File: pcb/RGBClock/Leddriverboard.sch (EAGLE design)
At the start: 37 parts, among them U1 LP3878MR-ADJ, U2 P82B96DR, U3 PCA9685PW, U4 ZXLD1362ET5TA, U5 ZXLD1362ET5TA, U6 ZXLD1362ET5TA, X1 5566-4

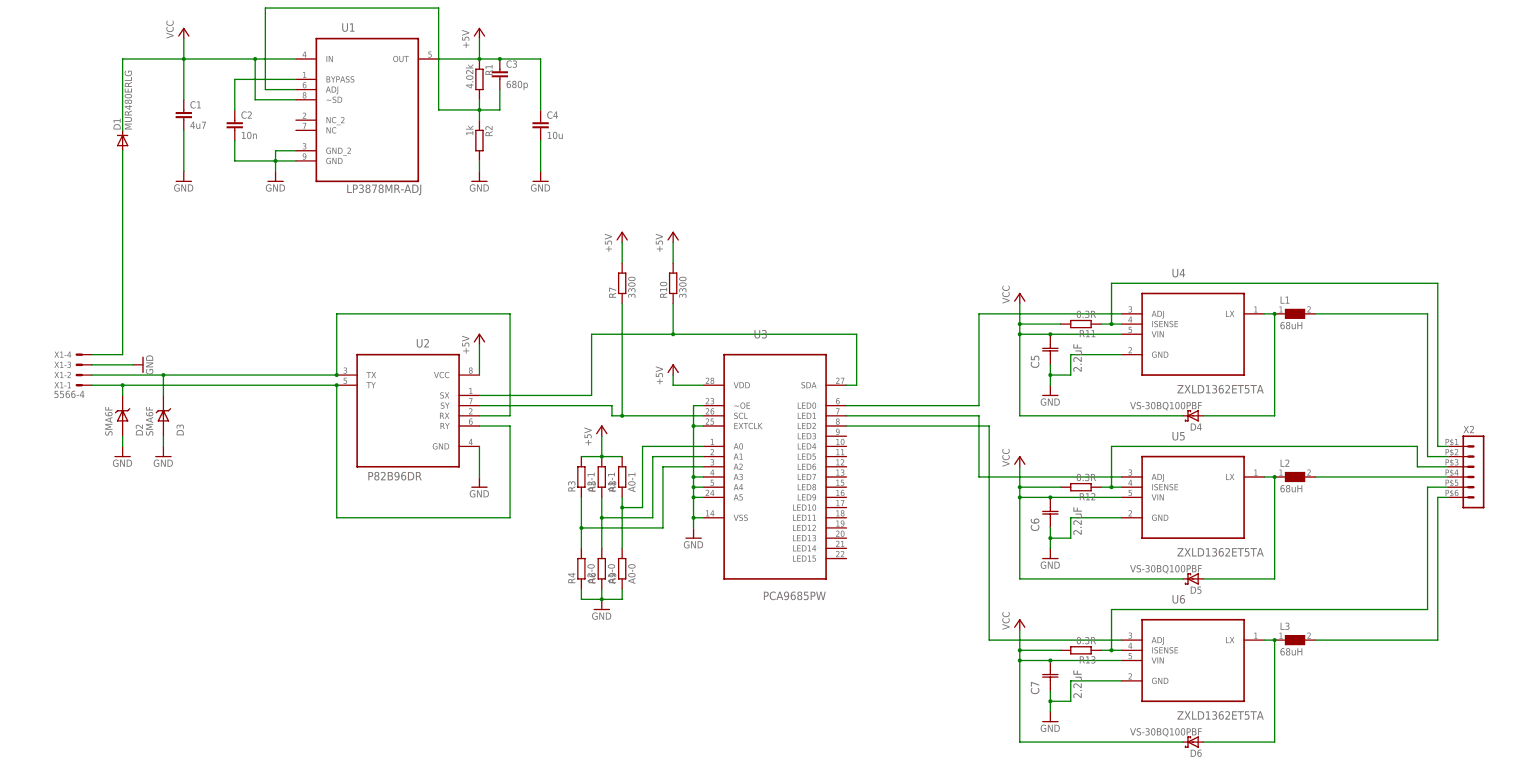
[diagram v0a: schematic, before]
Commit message: 
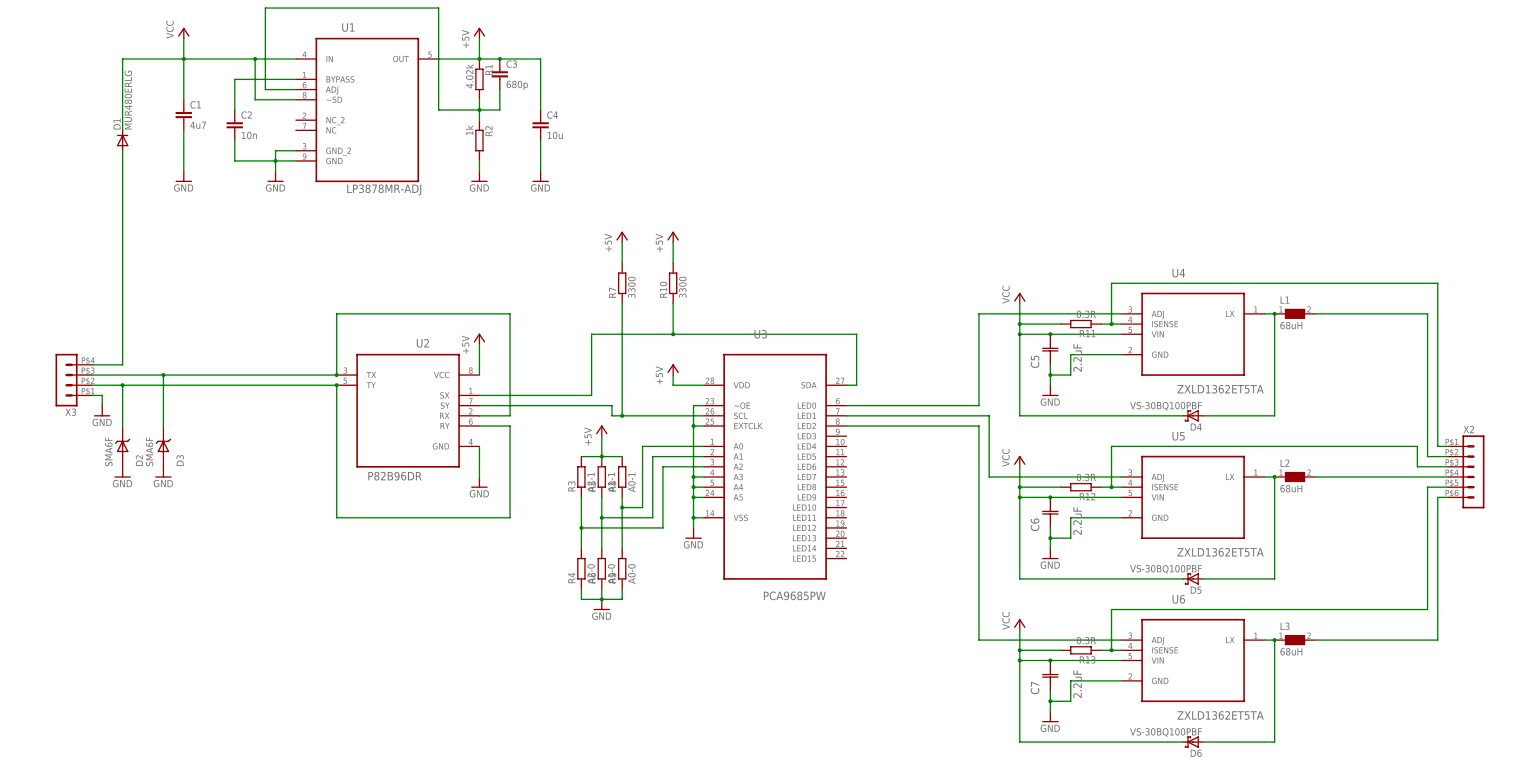
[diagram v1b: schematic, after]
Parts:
- removed X1: 5566-4, con-molex:5566-4
- added X3: (no value), con-molex-micro-fit-3_0:HEADER_POS4_43045-0401
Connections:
- net GND: now also X3.1; no longer X1-3.S
- net N$22: now also X3.2; no longer X1-1.S
- net N$25: now also X3.4; no longer X1-4.S
- net N$7: now also X3.3; no longer X1-2.S
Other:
- moved on the sheet: D2, D3
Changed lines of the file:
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@@
 <part name="GND14" library="supply1" deviceset="GND" device=""/>
 <part name="P+6" library="supply1" deviceset="+5V" device=""/>
-<part name="X1" library="con-molex" deviceset="5566-4" device=""/>
 <part name="D3" library="MyComponents" deviceset="SMA6F" device=""/>
 <part name="D2" library="MyComponents" deviceset="SMA6F" device=""/>
@@
 <part name="U1" library="Texas" deviceset="LP3878MR-ADJ" device=""/>
 <part name="P+3" library="supply1" deviceset="+5V" device=""/>
-<part name="GND15" library="supply1" deviceset="GND" device=""/>
 <part name="GND16" library="supply1" deviceset="GND" device=""/>
 <part name="C1" library="rcl" deviceset="C-EU" device="C1206" value="4u7"/>
@@
 <part name="R4" library="resistor" deviceset="R-EU_" device="R0402" value="A2-0"/>
 <part name="P+5" library="supply1" deviceset="+5V" device=""/>
+<part name="GND8" library="supply1" deviceset="GND" device=""/>
+<part name="X3" library="con-molex-micro-fit-3_0" deviceset="HEADER_POS4_?" device="43045-0401"/>
 </parts>
 <sheets>
@@
 <instance part="GND14" gate="1" x="-55.88" y="10.16"/>
 <instance part="P+6" gate="1" x="-55.88" y="48.26"/>
-<instance part="X1" gate="-1" x="-154.94" y="35.56" rot="R180"/>
-<instance part="X1" gate="-2" x="-154.94" y="38.1" rot="R180"/>
-<instance part="X1" gate="-3" x="-154.94" y="40.64" rot="R180"/>
-<instance part="X1" gate="-4" x="-154.94" y="43.18" rot="R180"/>
-<instance part="D3" gate="A" x="-134.62" y="27.94"/>
-<instance part="D2" gate="A" x="-144.78" y="27.94"/>
-<instance part="GND4" gate="1" x="-134.62" y="17.78"/>
-<instance part="GND5" gate="1" x="-144.78" y="17.78"/>
+<instance part="D3" gate="A" x="-134.62" y="20.32"/>
+<instance part="D2" gate="A" x="-144.78" y="20.32"/>
+<instance part="GND4" gate="1" x="-134.62" y="12.7"/>
+<instance part="GND5" gate="1" x="-144.78" y="12.7"/>
 <instance part="U1" gate="A" x="-83.82" y="106.68"/>
 <instance part="P+3" gate="1" x="-55.88" y="124.46"/>
-<instance part="GND15" gate="1" x="-139.7" y="40.64" rot="R90"/>
 <instance part="GND16" gate="1" x="-106.68" y="86.36"/>
 <instance part="C1" gate="G$1" x="-129.54" y="104.14"/>
@@
 <instance part="R4" gate="G$1" x="-30.48" y="-10.16" rot="R90"/>
 <instance part="P+5" gate="1" x="-25.4" y="25.4"/>
+<instance part="GND8" gate="1" x="-149.86" y="27.94"/>
+<instance part="X3" gate="G$1" x="-157.48" y="38.1" rot="R180"/>
 </instances>
 <busses>
@@
 <pinref part="D2" gate="A" pin="AN"/>
 <pinref part="GND5" gate="1" pin="GND"/>
-<wire x1="-144.78" y1="22.86" x2="-144.78" y2="20.32" width="0.1524" layer="91"/>
 </segment>
 <segment>
 <pinref part="D3" gate="A" pin="AN"/>
 <pinref part="GND4" gate="1" pin="GND"/>
-<wire x1="-134.62" y1="22.86" x2="-134.62" y2="20.32" width="0.1524" layer="91"/>
-</segment>
-<segment>
-<pinref part="X1" gate="-3" pin="S"/>
-<pinref part="GND15" gate="1" pin="GND"/>
-<wire x1="-152.4" y1="40.64" x2="-142.24" y2="40.64" width="0.1524" layer="91"/>
 </segment>
 <segment>
@@
 <wire x1="-25.4" y1="-15.24" x2="-25.4" y2="-17.78" width="0.1524" layer="91"/>
 <junction x="-25.4" y="-17.78"/>
+</segment>
+<segment>
+<pinref part="GND8" gate="1" pin="GND"/>
+<wire x1="-152.4" y1="33.02" x2="-149.86" y2="33.02" width="0.1524" layer="91"/>
+<wire x1="-149.86" y1="33.02" x2="-149.86" y2="30.48" width="0.1524" layer="91"/>
+<pinref part="X3" gate="G$1" pin="1"/>
 </segment>
 </net>
@@
 <segment>
 <pinref part="U5" gate="A" pin="ADJ"/>
-<wire x1="68.58" y1="12.7" x2="104.14" y2="12.7" width="0.1524" layer="91"/>
-<wire x1="68.58" y1="12.7" x2="68.58" y2="27.94" width="0.1524" layer="91"/>
+<wire x1="71.12" y1="12.7" x2="104.14" y2="12.7" width="0.1524" layer="91"/>
+<wire x1="71.12" y1="12.7" x2="71.12" y2="27.94" width="0.1524" layer="91"/>
 <pinref part="U3" gate="A" pin="LED1"/>
-<wire x1="68.58" y1="27.94" x2="35.56" y2="27.94" width="0.1524" layer="91"/>
+<wire x1="71.12" y1="27.94" x2="35.56" y2="27.94" width="0.1524" layer="91"/>
 </segment>
 </net>
@@
 <segment>
 <pinref part="U3" gate="A" pin="LED2"/>
-<wire x1="35.56" y1="25.4" x2="71.12" y2="25.4" width="0.1524" layer="91"/>
-<wire x1="71.12" y1="25.4" x2="71.12" y2="-27.94" width="0.1524" layer="91"/>
+<wire x1="35.56" y1="25.4" x2="68.58" y2="25.4" width="0.1524" layer="91"/>
+<wire x1="68.58" y1="25.4" x2="68.58" y2="-27.94" width="0.1524" layer="91"/>
 <pinref part="U6" gate="A" pin="ADJ"/>
-<wire x1="71.12" y1="-27.94" x2="104.14" y2="-27.94" width="0.1524" layer="91"/>
+<wire x1="68.58" y1="-27.94" x2="104.14" y2="-27.94" width="0.1524" layer="91"/>
 </segment>
 </net>
@@
 <pinref part="U2" gate="A" pin="RY"/>
 <wire x1="-48.26" y1="25.4" x2="-55.88" y2="25.4" width="0.1524" layer="91"/>
-<pinref part="X1" gate="-1" pin="S"/>
-<wire x1="-152.4" y1="35.56" x2="-144.78" y2="35.56" width="0.1524" layer="91"/>
 <pinref part="D2" gate="A" pin="KAT"/>
 <wire x1="-91.44" y1="35.56" x2="-144.78" y2="35.56" width="0.1524" layer="91"/>
-<wire x1="-144.78" y1="35.56" x2="-144.78" y2="33.02" width="0.1524" layer="91"/>
+<wire x1="-144.78" y1="35.56" x2="-144.78" y2="25.4" width="0.1524" layer="91"/>
+<junction x="-91.44" y="35.56"/>
+<wire x1="-144.78" y1="35.56" x2="-152.4" y2="35.56" width="0.1524" layer="91"/>
 <junction x="-144.78" y="35.56"/>
-<junction x="-91.44" y="35.56"/>
+<pinref part="X3" gate="G$1" pin="2"/>
 </segment>
 </net>
@@
 <pinref part="U2" gate="A" pin="RX"/>
 <wire x1="-55.88" y1="27.94" x2="-48.26" y2="27.94" width="0.1524" layer="91"/>
-<pinref part="X1" gate="-2" pin="S"/>
-<wire x1="-152.4" y1="38.1" x2="-134.62" y2="38.1" width="0.1524" layer="91"/>
 <pinref part="D3" gate="A" pin="KAT"/>
 <wire x1="-134.62" y1="38.1" x2="-91.44" y2="38.1" width="0.1524" layer="91"/>
-<wire x1="-134.62" y1="33.02" x2="-134.62" y2="38.1" width="0.1524" layer="91"/>
+<wire x1="-134.62" y1="25.4" x2="-134.62" y2="38.1" width="0.1524" layer="91"/>
+<junction x="-91.44" y="38.1"/>
+<wire x1="-134.62" y1="38.1" x2="-152.4" y2="38.1" width="0.1524" layer="91"/>
 <junction x="-134.62" y="38.1"/>
-<junction x="-91.44" y="38.1"/>
+<pinref part="X3" gate="G$1" pin="3"/>
 </segment>
 </net>
@@
 <segment>
 <pinref part="D1" gate="1" pin="A"/>
-<wire x1="-144.78" y1="93.98" x2="-144.78" y2="43.18" width="0.1524" layer="91"/>
-<pinref part="X1" gate="-4" pin="S"/>
-<wire x1="-144.78" y1="43.18" x2="-152.4" y2="43.18" width="0.1524" layer="91"/>
-</segment>
-</net>
+<wire x1="-144.78" y1="93.98" x2="-144.78" y2="40.64" width="0.1524" layer="91"/>
+<wire x1="-144.78" y1="40.64" x2="-152.4" y2="40.64" width="0.1524" layer="91"/>
+<pinref part="X3" gate="G$1" pin="4"/>
+</segment>
+</net>

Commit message: 
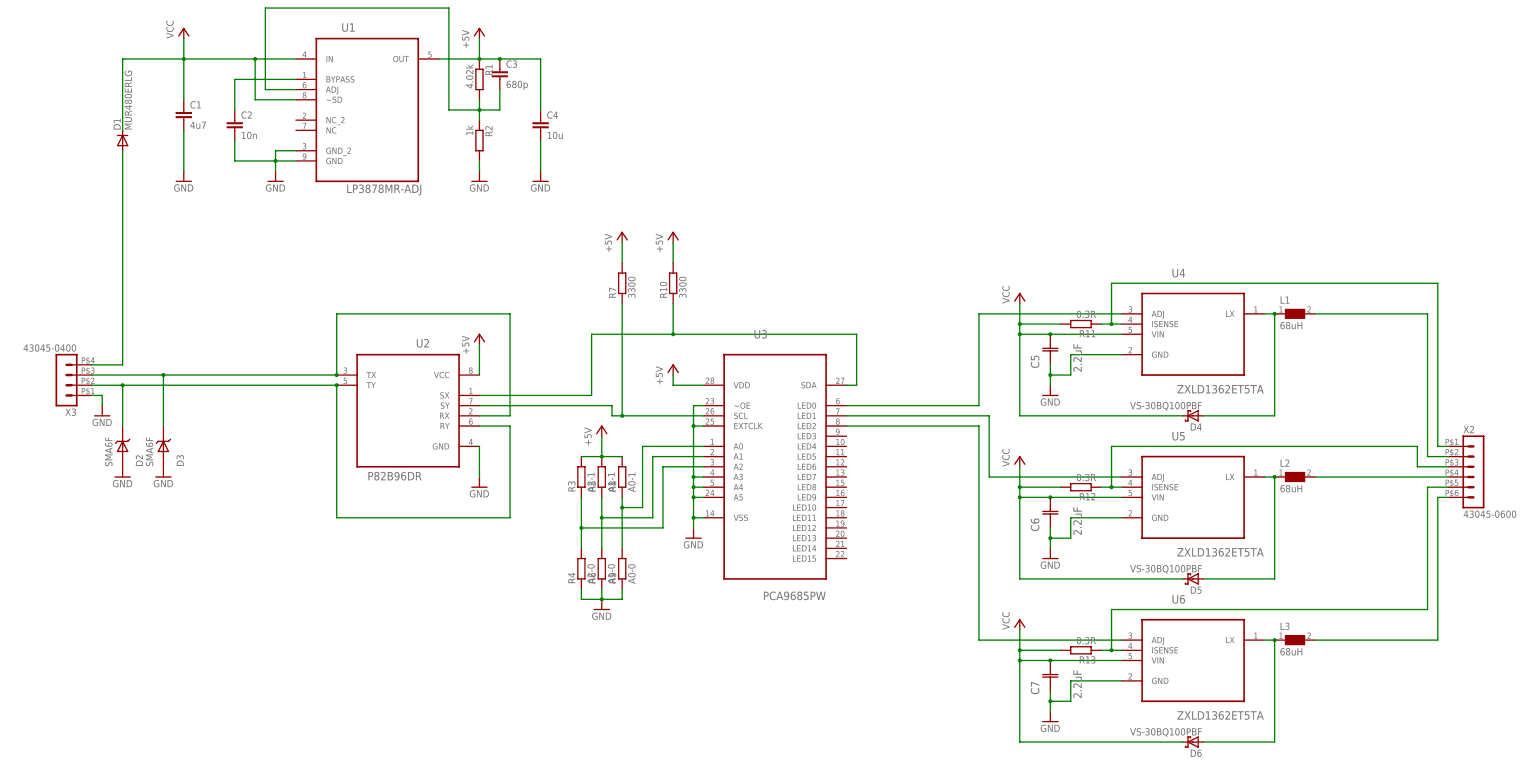
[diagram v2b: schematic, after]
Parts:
- X2: value (none) -> 43045-0600
- X3: value (none) -> 43045-0400
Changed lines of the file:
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@@
 <part name="P+14" library="supply1" deviceset="+5V" device=""/>
 <part name="P+4" library="supply1" deviceset="VCC" device=""/>
-<part name="X2" library="con-molex-micro-fit-3_0" deviceset="HEADER_POS6_?" device="43045-0600"/>
+<part name="X2" library="con-molex-micro-fit-3_0" deviceset="HEADER_POS6_?" device="43045-0600" value="43045-0600"/>
 <part name="D4" library="MyComponents" deviceset="VS-30BQ100PBF" device=""/>
 <part name="D5" library="MyComponents" deviceset="VS-30BQ100PBF" device=""/>
@@
 <part name="P+5" library="supply1" deviceset="+5V" device=""/>
 <part name="GND8" library="supply1" deviceset="GND" device=""/>
-<part name="X3" library="con-molex-micro-fit-3_0" deviceset="HEADER_POS4_?" device="43045-0401"/>
+<part name="X3" library="con-molex-micro-fit-3_0" deviceset="HEADER_POS4_?" device="43045-0401" value="43045-0400"/>
 </parts>
 <sheets>
@@
 <wire x1="-50.8" y1="109.22" x2="-50.8" y2="104.14" width="0.1524" layer="91"/>
 <wire x1="-50.8" y1="104.14" x2="-55.88" y2="104.14" width="0.1524" layer="91"/>
-<wire x1="-55.88" y1="104.14" x2="-66.04" y2="104.14" width="0.1524" layer="91"/>
-<wire x1="-66.04" y1="104.14" x2="-66.04" y2="129.54" width="0.1524" layer="91"/>
-<wire x1="-66.04" y1="129.54" x2="-109.22" y2="129.54" width="0.1524" layer="91"/>
+<wire x1="-55.88" y1="104.14" x2="-63.5" y2="104.14" width="0.1524" layer="91"/>
+<wire x1="-63.5" y1="104.14" x2="-63.5" y2="129.54" width="0.1524" layer="91"/>
+<wire x1="-63.5" y1="129.54" x2="-109.22" y2="129.54" width="0.1524" layer="91"/>
 <wire x1="-109.22" y1="129.54" x2="-109.22" y2="109.22" width="0.1524" layer="91"/>
 <pinref part="U1" gate="A" pin="ADJ"/>
